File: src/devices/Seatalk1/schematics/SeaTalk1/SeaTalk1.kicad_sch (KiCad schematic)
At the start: 30 parts, among them J1 Raspberry_Pi_2_3, J3 Conn_01x03_Pin, Q1 BC557, Q2 BC547, Q3 BC547, Q4 BC547, Q5 BC547, Q6 BC547

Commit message: Schema cleanup
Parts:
- R12, V2, V_TXD1: now left out of the parts list
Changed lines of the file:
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@@
   (junction (at 78.74 91.44) (diameter 0) (color 0 0 0 0)
   )
-  (junction (at 55.88 67.31) (diameter 0) (color 0 0 0 0)
-  )
   (junction (at 104.14 91.44) (diameter 0) (color 0 0 0 0)
   )
@@
     (stroke (width 0) (type default))
   )
+  (wire (pts (xy 148.59 19.05) (xy 238.76 19.05))
+    (stroke (width 0) (type default))
+  )
   (wire (pts (xy 93.98 71.12) (xy 104.14 71.12))
     (stroke (width 0) (type default))
@@
     (stroke (width 0) (type default))
   )
+  (wire (pts (xy 233.68 22.86) (xy 233.68 25.4))
+    (stroke (width 0) (type default))
+  )
+  (wire (pts (xy 148.59 38.1) (xy 148.59 57.15))
+    (stroke (width 0) (type default))
+  )
   (wire (pts (xy 134.62 91.44) (xy 148.59 91.44))
     (stroke (width 0) (type default))
   )
-  (wire (pts (xy 233.68 22.86) (xy 233.68 25.4))
-    (stroke (width 0) (type default))
-  )
-  (wire (pts (xy 148.59 38.1) (xy 148.59 57.15))
-    (stroke (width 0) (type default))
-  )
   (wire (pts (xy 134.62 58.42) (xy 134.62 91.44))
     (stroke (width 0) (type default))
@@
     (stroke (width 0) (type default))
   )
-  (wire (pts (xy 46.99 67.31) (xy 55.88 67.31))
-    (stroke (width 0) (type default))
-  )
   (wire (pts (xy 262.89 140.97) (xy 262.89 161.29))
     (stroke (width 0) (type default))
@@
   )
   (wire (pts (xy 71.12 53.34) (xy 71.12 67.31))
-    (stroke (width 0) (type default))
-  )
-  (wire (pts (xy 148.59 19.05) (xy 238.76 19.05))
     (stroke (width 0) (type default))
   )
@@
     )
   )
-  (global_label "SIM_BUS" (shape output) (at 224.79 116.84 90) (fields_autoplaced)
+  (global_label "SEATALK" (shape output) (at 224.79 116.84 90) (fields_autoplaced)
     (effects (font (size 1.27 1.27)) (justify left))
-    (property "Intersheetrefs" "${INTERSHEET_REFS}" (at 224.79 105.8115 90)
+    (property "Intersheetrefs" "${INTERSHEET_REFS}" (at 224.79 106.0534 90)
       (effects (font (size 1.27 1.27)) (justify left) hide)
     )
@@
     )
   )
-  (global_label "SIM_BUS" (shape input) (at 46.99 67.31 180) (fields_autoplaced)
-    (effects (font (size 1.27 1.27)) (justify right))
-    (property "Intersheetrefs" "${INTERSHEET_REFS}" (at 35.9615 67.31 0)
-      (effects (font (size 1.27 1.27)) (justify right) hide)
-    )
-  )
   (global_label "VCC_3.3" (shape passive) (at 236.22 118.11 90) (fields_autoplaced)
     (effects (font (size 1.27 1.27)) (justify left))
@@
   )
   (symbol (lib_id "Simulation_SPICE:VDC") (at 22.86 64.77 0) (unit 1)
-    (in_bom yes) (on_board yes) (dnp no) (fields_autoplaced)
+    (in_bom no) (on_board no) (dnp no) (fields_autoplaced)
     (property "Reference" "V2" (at 26.67 63.3702 0)
       (effects (font (size 1.27 1.27)) (justify left))
@@
       (effects (font (size 1.27 1.27)) (justify left) hide)
     )
-    (property "Sim.Params" "y1=12 y2=2 td=1m tr=2n tf=2n tw=1m per=2m np=3" (at 228.6 144.6502 0)
+    (property "Sim.Params" "y1=12 y2=2 td=1m tr=2n tf=2n tw=0.2m per=2m np=3" (at 228.6 144.6502 0)
       (effects (font (size 1.27 1.27)) (justify left))
     )
@@
   )
   (symbol (lib_id "Device:R") (at 57.15 30.48 270) (unit 1)
-    (in_bom yes) (on_board yes) (dnp no) (fields_autoplaced)
+    (in_bom no) (on_board no) (dnp no) (fields_autoplaced)
     (property "Reference" "R12" (at 57.15 24.13 90)
       (effects (font (size 1.27 1.27)))
@@
       (effects (font (size 1.27 1.27)) hide)
     )
-    (property "Sim.Pins" "1=A 2=K" (at 134.62 39.37 0)
-      (effects (font (size 1.27 1.27)) hide)
-    )
-    (property "Sim.Params" "is=259.39f rs=0.24229 n=4.0113 ikf=0 eg=3 xtitun=25" (at 134.62 39.37 0)
+    (property "Sim.Pins" "1=K 2=A" (at 134.62 39.37 0)
+      (effects (font (size 1.27 1.27)) hide)
+    )
+    (property "Sim.Params" "is=259390a" (at 134.62 39.37 0)
+      (effects (font (size 1.27 1.27)) hide)
+    )
+    (property "Sim.Library" "Leds.lib" (at 134.62 39.37 0)
+      (effects (font (size 1.27 1.27)) hide)
+    )
+    (property "Sim.Name" "DLED_Nichia" (at 134.62 39.37 0)
       (effects (font (size 1.27 1.27)) hide)
     )
@@
   )
   (symbol (lib_id "Simulation_SPICE:VPULSE") (at 262.89 135.89 0) (unit 1)
-    (in_bom yes) (on_board yes) (dnp no) (fields_autoplaced)
+    (in_bom no) (on_board no) (dnp no) (fields_autoplaced)
     (property "Reference" "V_TXD1" (at 266.7 133.2202 0)
       (effects (font (size 1.27 1.27)) (justify left))

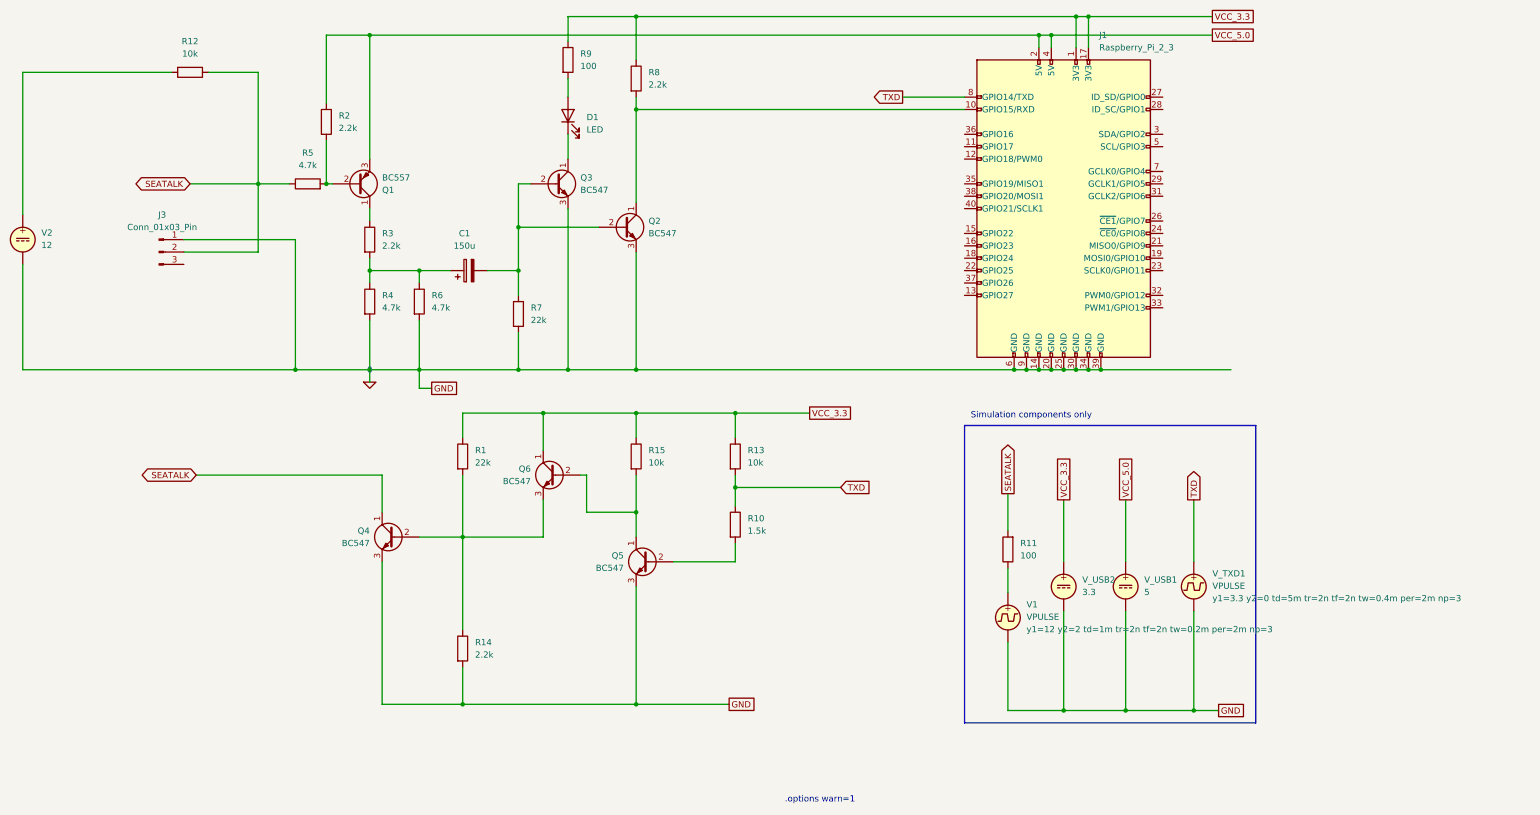
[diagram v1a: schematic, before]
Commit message: Minor cleanup, create empty PCB
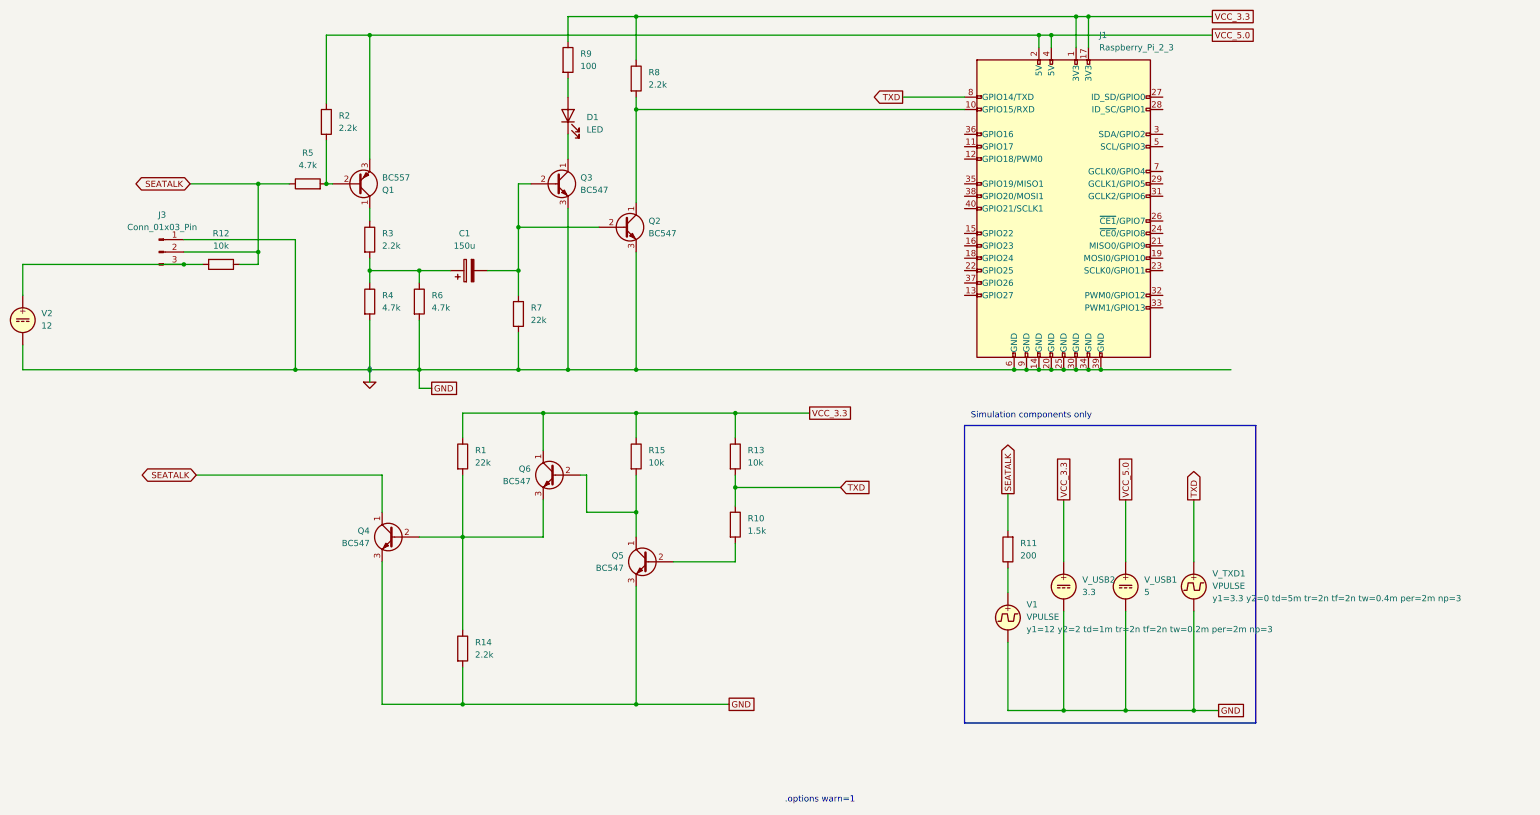
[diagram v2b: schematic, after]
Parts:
- C1: footprint Capacitor_THT:CP_Radial_D10.0mm_P5.00mm -> Capacitor_THT:CP_Radial_D12.5mm_P7.50mm
- R1, R12, R13, R14, R15, R2, R3, R4, R5, R6, R7, R8: footprint (none) -> Resistor_THT:R_Axial_DIN0309_L9.0mm_D3.2mm_P15.24mm_Horizontal
- R11: value 100 -> 200
- R9: footprint Resistor_THT:R_Axial_DIN0414_L11.9mm_D4.5mm_P15.24mm_Horizontal -> Resistor_THT:R_Axial_DIN0309_L9.0mm_D3.2mm_P15.24mm_Horizontal
- V1: now left out of the parts list
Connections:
- net at R12.2, V2.1: now also J3.3 (Pin_3)
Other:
- moved on the sheet: R12, V2
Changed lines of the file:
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@@
   (junction (at 124.46 91.44) (diameter 0) (color 0 0 0 0)
   )
+  (junction (at 55.88 69.85) (diameter 0) (color 0 0 0 0)
+  )
   (junction (at 233.68 22.86) (diameter 0) (color 0 0 0 0)
   )
   (junction (at 238.76 91.44) (diameter 0) (color 0 0 0 0)
   )
+  (junction (at 71.12 67.31) (diameter 0) (color 0 0 0 0)
+  )
   (junction (at 262.89 161.29) (diameter 0) (color 0 0 0 0)
   )
@@
     (stroke (width 0) (type default))
   )
+  (wire (pts (xy 22.86 86.36) (xy 22.86 91.44))
+    (stroke (width 0) (type default))
+  )
   (wire (pts (xy 238.76 19.05) (xy 238.76 25.4))
     (stroke (width 0) (type default))
@@
     (stroke (width 0) (type default))
   )
-  (wire (pts (xy 71.12 30.48) (xy 71.12 53.34))
+  (wire (pts (xy 71.12 69.85) (xy 71.12 67.31))
     (stroke (width 0) (type default))
   )
@@
     (stroke (width 0) (type default))
   )
-  (wire (pts (xy 22.86 30.48) (xy 22.86 59.69))
+  (wire (pts (xy 22.86 69.85) (xy 22.86 76.2))
     (stroke (width 0) (type default))
   )
@@
     (stroke (width 0) (type default))
   )
+  (wire (pts (xy 22.86 69.85) (xy 55.88 69.85))
+    (stroke (width 0) (type default))
+  )
   (wire (pts (xy 248.92 118.11) (xy 248.92 130.81))
     (stroke (width 0) (type default))
   )
-  (wire (pts (xy 22.86 69.85) (xy 22.86 91.44))
-    (stroke (width 0) (type default))
-  )
   (wire (pts (xy 93.98 81.28) (xy 93.98 91.44))
     (stroke (width 0) (type default))
@@
     (stroke (width 0) (type default))
   )
+  (wire (pts (xy 55.88 69.85) (xy 59.69 69.85))
+    (stroke (width 0) (type default))
+  )
   (wire (pts (xy 129.54 125.73) (xy 113.03 125.73))
     (stroke (width 0) (type default))
@@
     (stroke (width 0) (type default))
   )
-  (wire (pts (xy 71.12 53.34) (xy 71.12 67.31))
-    (stroke (width 0) (type default))
-  )
   (wire (pts (xy 78.74 64.77) (xy 78.74 91.44))
     (stroke (width 0) (type default))
@@
     (stroke (width 0) (type default))
   )
+  (wire (pts (xy 71.12 67.31) (xy 71.12 53.34))
+    (stroke (width 0) (type default))
+  )
   (wire (pts (xy 236.22 161.29) (xy 248.92 161.29))
     (stroke (width 0) (type default))
@@
     (stroke (width 0) (type default))
   )
-  (wire (pts (xy 60.96 30.48) (xy 71.12 30.48))
+  (wire (pts (xy 67.31 69.85) (xy 71.12 69.85))
     (stroke (width 0) (type default))
   )
@@
   )
   (wire (pts (xy 96.52 130.81) (xy 96.52 160.02))
-    (stroke (width 0) (type default))
-  )
-  (wire (pts (xy 53.34 30.48) (xy 22.86 30.48))
     (stroke (width 0) (type default))
   )
@@
       (effects (font (size 1.27 1.27)) (justify left))
     )
-    (property "Footprint" "" (at 146.812 31.75 90)
+    (property "Footprint" "Resistor_THT:R_Axial_DIN0309_L9.0mm_D3.2mm_P15.24mm_Horizontal" (at 146.812 31.75 90)
       (effects (font (size 1.27 1.27)) hide)
     )
@@
       (effects (font (size 1.27 1.27)) (justify left))
     )
-    (property "Footprint" "" (at 92.202 64.77 90)
+    (property "Footprint" "Resistor_THT:R_Axial_DIN0309_L9.0mm_D3.2mm_P15.24mm_Horizontal" (at 92.202 64.77 90)
       (effects (font (size 1.27 1.27)) hide)
     )
@@
       (effects (font (size 1.27 1.27)) (justify left))
     )
-    (property "Footprint" "" (at 122.682 80.01 90)
+    (property "Footprint" "Resistor_THT:R_Axial_DIN0309_L9.0mm_D3.2mm_P15.24mm_Horizontal" (at 122.682 80.01 90)
       (effects (font (size 1.27 1.27)) hide)
     )
@@
       (effects (font (size 1.27 1.27)) (justify right))
     )
-    (property "Value" "100" (at 227.33 129.54 0)
+    (property "Value" "200" (at 227.33 129.54 0)
       (effects (font (size 1.27 1.27)) (justify right))
     )
@@
     )
   )
-  (symbol (lib_id "Simulation_SPICE:VDC") (at 22.86 64.77 0) (unit 1)
+  (symbol (lib_id "Simulation_SPICE:VDC") (at 22.86 81.28 0) (unit 1)
     (in_bom no) (on_board no) (dnp no) (fields_autoplaced)
-    (property "Reference" "V2" (at 26.67 63.3702 0)
-      (effects (font (size 1.27 1.27)) (justify left))
-    )
-    (property "Value" "12" (at 26.67 65.9102 0)
-      (effects (font (size 1.27 1.27)) (justify left))
-    )
-    (property "Footprint" "" (at 22.86 64.77 0)
-      (effects (font (size 1.27 1.27)) hide)
-    )
-    (property "Datasheet" "~" (at 22.86 64.77 0)
-      (effects (font (size 1.27 1.27)) hide)
-    )
-    (property "Sim.Pins" "1=+ 2=-" (at 22.86 64.77 0)
-      (effects (font (size 1.27 1.27)) hide)
-    )
-    (property "Sim.Type" "DC" (at 22.86 64.77 0)
-      (effects (font (size 1.27 1.27)) hide)
-    )
-    (property "Sim.Device" "V" (at 22.86 64.77 0)
+    (property "Reference" "V2" (at 26.67 79.8802 0)
+      (effects (font (size 1.27 1.27)) (justify left))
+    )
+    (property "Value" "12" (at 26.67 82.4202 0)
+      (effects (font (size 1.27 1.27)) (justify left))
+    )
+    (property "Footprint" "" (at 22.86 81.28 0)
+      (effects (font (size 1.27 1.27)) hide)
+    )
+    (property "Datasheet" "~" (at 22.86 81.28 0)
+      (effects (font (size 1.27 1.27)) hide)
+    )
+    (property "Sim.Pins" "1=+ 2=-" (at 22.86 81.28 0)
+      (effects (font (size 1.27 1.27)) hide)
+    )
+    (property "Sim.Type" "DC" (at 22.86 81.28 0)
+      (effects (font (size 1.27 1.27)) hide)
+    )
+    (property "Sim.Device" "V" (at 22.86 81.28 0)
       (effects (font (size 1.27 1.27)) (justify left) hide)
     )
@@
       (effects (font (size 1.27 1.27)) (justify left))
     )
-    (property "Footprint" "" (at 102.362 77.47 90)
+    (property "Footprint" "Resistor_THT:R_Axial_DIN0309_L9.0mm_D3.2mm_P15.24mm_Horizontal" (at 102.362 77.47 90)
       (effects (font (size 1.27 1.27)) hide)
     )
@@
   )
   (symbol (lib_id "Simulation_SPICE:VPULSE") (at 224.79 142.24 0) (unit 1)
-    (in_bom yes) (on_board yes) (dnp no) (fields_autoplaced)
+    (in_bom no) (on_board no) (dnp no) (fields_autoplaced)
     (property "Reference" "V1" (at 228.6 139.5702 0)
       (effects (font (size 1.27 1.27)) (justify left))
@@
     )
   )
-  (symbol (lib_id "Device:R") (at 57.15 30.48 270) (unit 1)
+  (symbol (lib_id "Device:R") (at 63.5 69.85 270) (unit 1)
     (in_bom no) (on_board no) (dnp no) (fields_autoplaced)
-    (property "Reference" "R12" (at 57.15 24.13 90)
+    (property "Reference" "R12" (at 63.5 63.5 90)
       (effects (font (size 1.27 1.27)))
     )
-    (property "Value" "10k" (at 57.15 26.67 90)
+    (property "Value" "10k" (at 63.5 66.04 90)
       (effects (font (size 1.27 1.27)))
     )
-    (property "Footprint" "" (at 57.15 28.702 90)
-      (effects (font (size 1.27 1.27)) hide)
-    )
-    (property "Datasheet" "~" (at 57.15 30.48 0)
-      (effects (font (size 1.27 1.27)) hide)
-    )
-    (property "Remarks" "External pull-up from bus" (at 57.15 30.48 90)
+    (property "Footprint" "Resistor_THT:R_Axial_DIN0309_L9.0mm_D3.2mm_P15.24mm_Horizontal" (at 63.5 68.072 90)
+      (effects (font (size 1.27 1.27)) hide)
+    )
+    (property "Datasheet" "~" (at 63.5 69.85 0)
+      (effects (font (size 1.27 1.27)) hide)
+    )
+    (property "Remarks" "External pull-up from bus" (at 63.5 69.85 90)
       (effects (font (size 1.27 1.27)) hide)
     )
@@
       (effects (font (size 1.27 1.27)) (justify left))
     )
-    (property "Footprint" "Resistor_THT:R_Axial_DIN0414_L11.9mm_D4.5mm_P15.24mm_Horizontal" (at 132.842 27.94 90)
+    (property "Footprint" "Resistor_THT:R_Axial_DIN0309_L9.0mm_D3.2mm_P15.24mm_Horizontal" (at 132.842 27.94 90)
       (effects (font (size 1.27 1.27)) hide)
     )
@@
       (effects (font (size 1.27 1.27)) (justify left))
     )
-    (property "Footprint" "" (at 92.202 77.47 90)
+    (property "Footprint" "Resistor_THT:R_Axial_DIN0309_L9.0mm_D3.2mm_P15.24mm_Horizontal" (at 92.202 77.47 90)
       (effects (font (size 1.27 1.27)) hide)
     )
@@
       (effects (font (size 1.27 1.27)) (justify left))
     )
-    (property "Footprint" "" (at 111.252 148.59 90)
+    (property "Footprint" "Resistor_THT:R_Axial_DIN0309_L9.0mm_D3.2mm_P15.24mm_Horizontal" (at 111.252 148.59 90)
       (effects (font (size 1.27 1.27)) hide)
     )
@@
       (effects (font (size 1.27 1.27)) (justify left))
     )
-    (property "Footprint" "" (at 146.812 109.22 90)
+    (property "Footprint" "Resistor_THT:R_Axial_DIN0309_L9.0mm_D3.2mm_P15.24mm_Horizontal" (at 146.812 109.22 90)
       (effects (font (size 1.27 1.27)) hide)
     )
@@
       (effects (font (size 1.27 1.27)) (justify left))
     )
-    (property "Footprint" "" (at 167.132 109.22 90)
+    (property "Footprint" "Resistor_THT:R_Axial_DIN0309_L9.0mm_D3.2mm_P15.24mm_Horizontal" (at 167.132 109.22 90)
       (effects (font (size 1.27 1.27)) hide)
     )
@@
       (effects (font (size 1.27 1.27)) (justify left))
     )
-    (property "Footprint" "" (at 111.252 109.22 90)
+    (property "Footprint" "Resistor_THT:R_Axial_DIN0309_L9.0mm_D3.2mm_P15.24mm_Horizontal" (at 111.252 109.22 90)
       (effects (font (size 1.27 1.27)) hide)
     )
@@
       (effects (font (size 1.27 1.27)))
     )
-    (property "Footprint" "" (at 81.28 55.118 90)
+    (property "Footprint" "Resistor_THT:R_Axial_DIN0309_L9.0mm_D3.2mm_P15.24mm_Horizontal" (at 81.28 55.118 90)
       (effects (font (size 1.27 1.27)) hide)
     )
@@
       (effects (font (size 1.27 1.27)) (justify left))
     )
-    (property "Footprint" "" (at 83.312 40.64 90)
+    (property "Footprint" "Resistor_THT:R_Axial_DIN0309_L9.0mm_D3.2mm_P15.24mm_Horizontal" (at 83.312 40.64 90)
       (effects (font (size 1.27 1.27)) hide)
     )
@@
       (effects (font (size 1.27 1.27)))
     )
-    (property "Footprint" "Capacitor_THT:CP_Radial_D10.0mm_P5.00mm" (at 118.11 70.1548 0)
-      (effects (font (size 1.27 1.27)) hide)
-    )
+    (property "Footprint" "Capacitor_THT:CP_Radial_D12.5mm_P7.50mm" (at 118.11 70.1548 0)
+      (effects (font (size 1.27 1.27)) hide)
+    )
